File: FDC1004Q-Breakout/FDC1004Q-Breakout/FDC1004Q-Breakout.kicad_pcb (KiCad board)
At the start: 2 copper layers, 14.6 x 12.3 mm, 4 parts, among them J1 Breakout, J2 Sense, U1 FDC1004DGSR

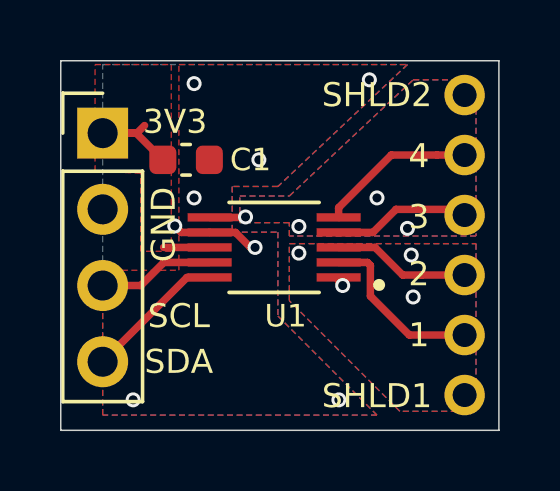
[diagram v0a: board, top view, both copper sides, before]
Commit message: Minor updates to AD7156, FDC1004Q
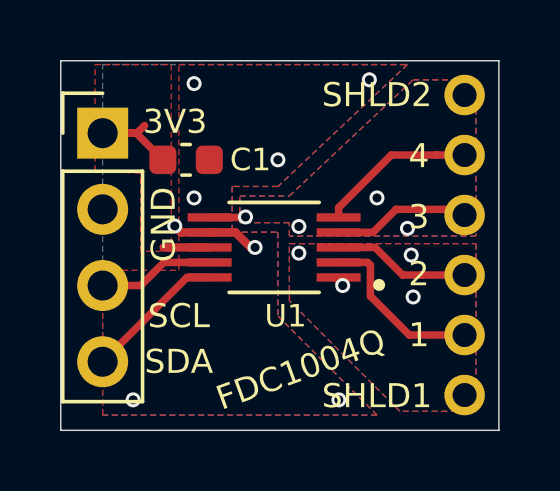
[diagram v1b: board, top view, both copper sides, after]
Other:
- net class Default removed
- board text added: "FDC1004Q"
